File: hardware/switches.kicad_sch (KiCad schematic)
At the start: 5 parts, among them SW601 SW_Push, SW602 SW_Push, SW603 SW_Push, SW604 SW_Push, SW605 SW_Push

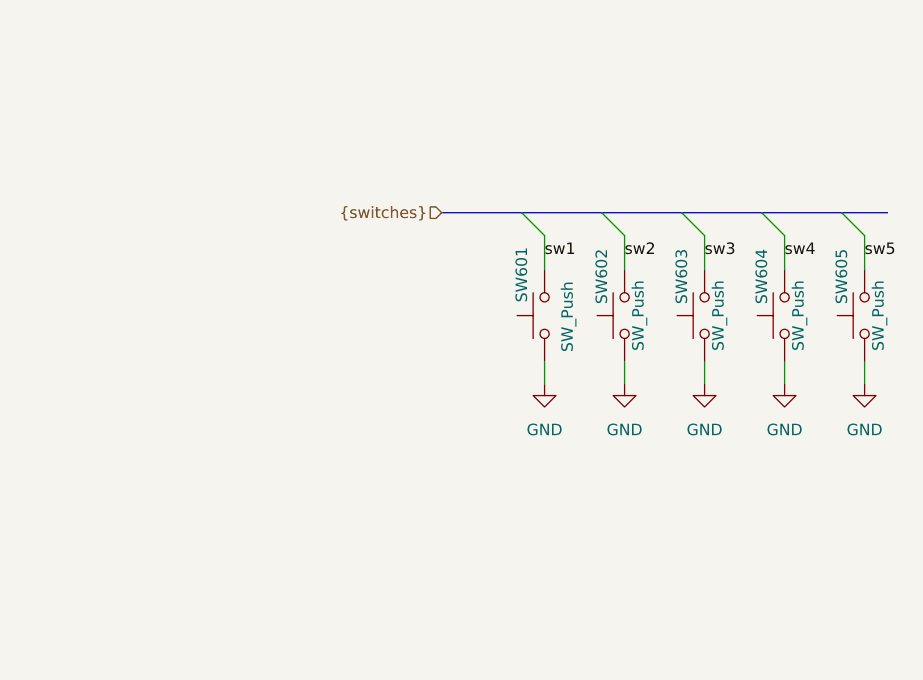
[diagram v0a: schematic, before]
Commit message: update board file, made similar to OS solenoid decoder
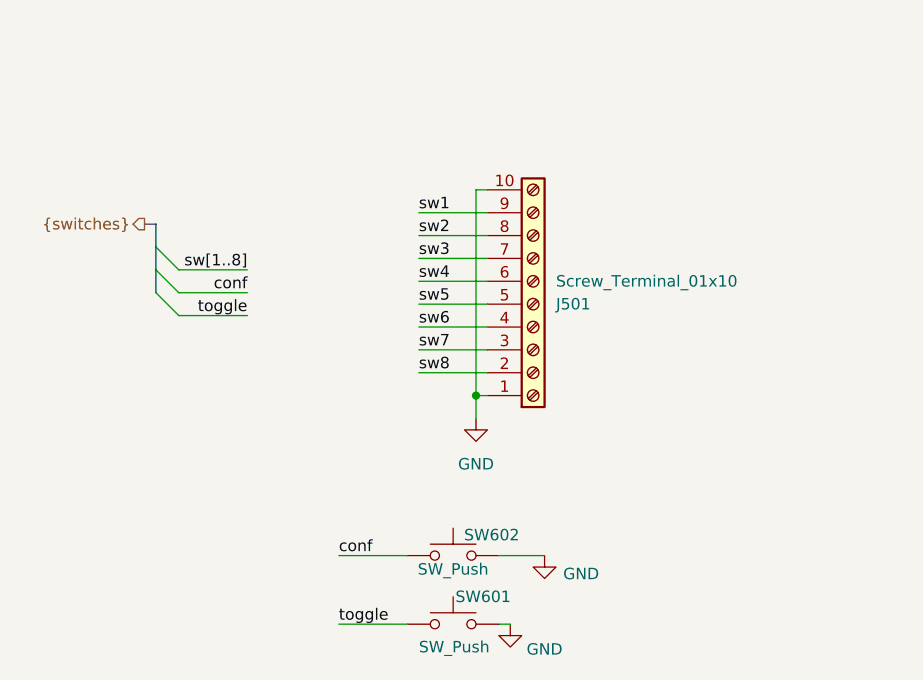
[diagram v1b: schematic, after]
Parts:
- removed SW603, SW604, SW605: SW_Push, custom_kicad_lib_sk:tactile_SMD_6mm, symbol custom_kicad_lib_sk:tactile_SMD_6mm
- added J501: Screw_Terminal_01x10, TerminalBlock_Phoenix:TerminalBlock_Phoenix_MPT-0,5-10-2.54_1x10_P2.54mm_Horizontal, symbol Connector:Screw_Terminal_01x10
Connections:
- net GND: now also J501.1 (Pin_1), J501.10 (Pin_10)
- net sw1: now also J501.9 (Pin_9); no longer SW601.2
- net sw2: now also J501.8 (Pin_8); no longer SW602.2
- net sw3: now also J501.7 (Pin_7)
- net sw4: now also J501.6 (Pin_6)
- net sw5: now also J501.5 (Pin_5)
- new net conf: SW602.2
- new net sw6: J501.4 (Pin_4)
- new net sw7: J501.3 (Pin_3)
- new net sw8: J501.2 (Pin_2)
- new net toggle: SW601.2
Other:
- moved on the sheet: SW601, SW602

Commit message: added manual and picture
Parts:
- added D505, D506, D507, D508, D509, D510, D511, D512: LED, LED_SMD:LED_0805_2012Metric_Pad1.15x1.40mm_HandSolder, symbol custom_kicad_lib_sk:LED
- added R501, R502, R503, R504, R505, R506, R507, R508: 1k, custom_kicad_lib_sk:R_0603_smalltext, symbol resistors_0603:R_1k_0603
- J501: JLCPCB Part# (none) -> C474928
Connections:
- net sw1: now also D505.1 (K)
- net sw2: now also D506.1 (K)
- net sw3: now also D507.1 (K)
- net sw4: now also D508.1 (K)
- net sw5: now also D509.1 (K)
- net sw6: now also D510.1 (K)
- net sw7: now also D511.1 (K)
- net sw8: now also D512.1 (K)
- new net: D512.2 (A), R508.2
- new net: D510.2 (A), R506.2
- new net: D509.2 (A), R505.2
- new net: D507.2 (A), R503.2
- new net: D508.2 (A), R504.2
- new net: D511.2 (A), R507.2
- new net: D505.2 (A), R501.2
- new net: D506.2 (A), R502.2
- new net +5V: R501.1, R502.1, R503.1, R504.1, R505.1, R506.1, R507.1, R508.1
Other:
- moved on the sheet: J501

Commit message: added translations
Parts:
- removed D505, D506, D507, D508, D509, D510, D511, D512: LED, LED_SMD:LED_0805_2012Metric_Pad1.15x1.40mm_HandSolder, symbol custom_kicad_lib_sk:LED
- removed J501: Screw_Terminal_01x10, TerminalBlock_Phoenix:TerminalBlock_Phoenix_MPT-0,5-10-2.54_1x10_P2.54mm_Horizontal, symbol Connector:Screw_Terminal_01x10
- removed R501, R502, R503, R504, R505, R506, R507, R508: 1k, custom_kicad_lib_sk:R_0603_smalltext, symbol resistors_0603:R_1k_0603
